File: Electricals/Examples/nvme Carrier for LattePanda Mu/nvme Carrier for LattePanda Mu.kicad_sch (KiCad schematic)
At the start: 8 parts

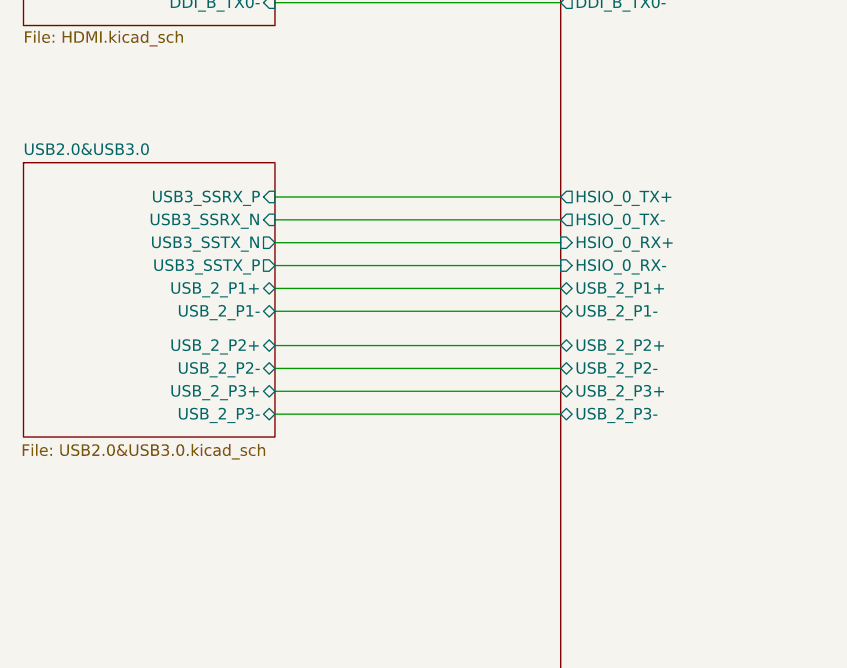
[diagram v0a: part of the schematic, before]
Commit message: Layout optimization + internal USB
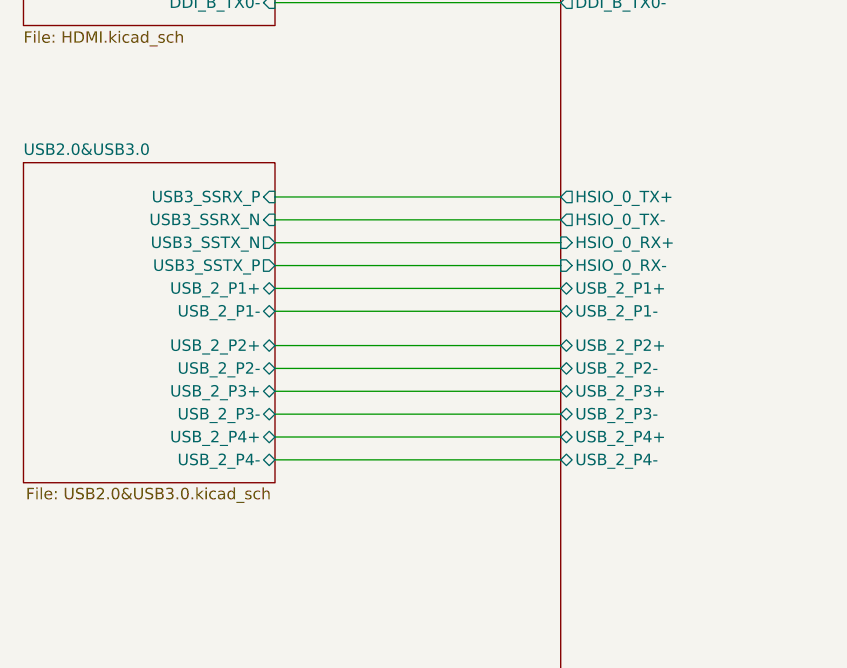
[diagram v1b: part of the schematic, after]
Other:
- sheet LattePanda Module ports: added USB_2_P4+, USB_2_P4-; removed none
- sheet USB2.0&USB3.0 ports: added USB_2_P4+, USB_2_P4-; removed none
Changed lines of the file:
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@@
 	(wire
 		(pts
+			(xy 195.58 242.57) (xy 227.33 242.57)
+		)
+		(stroke
+			(width 0)
+			(type default)
+		)
+	)
+	(wire
+		(pts
 			(xy 227.33 186.69) (xy 195.58 186.69)
 		)
@@
 	(wire
 		(pts
+			(xy 195.58 240.03) (xy 227.33 240.03)
+		)
+		(stroke
+			(width 0)
+			(type default)
+		)
+	)
+	(wire
+		(pts
 			(xy 227.33 184.15) (xy 195.58 184.15)
 		)
@@
 			)
 		)
+		(pin "USB_2_P4+" bidirectional
+			(at 227.33 240.03 180)
+			(effects
+				(font
+					(size 1.27 1.27)
+				)
+				(justify left)
+			)
+		)
+		(pin "USB_2_P4-" bidirectional
+			(at 227.33 242.57 180)
+			(effects
+				(font
+					(size 1.27 1.27)
+				)
+				(justify left)
+			)
+		)
 		(instances
 			(project "nvme Carrier for LattePanda Mu"
@@
 	(sheet
 		(at 167.64 209.55)
-		(size 27.94 30.48)
+		(size 27.94 35.56)
 		(stroke
 			(width 0.1524)
@@
 		)
 		(property "Sheetfile" "USB2.0&USB3.0.kicad_sch"
-			(at 167.386 240.792 0)
+			(at 167.894 245.618 0)
 			(effects
 				(font
@@
 			(effects
 				(font
+					(size 1.27 1.27)
+				)
+				(justify right)
+			)
+		)
+		(pin "USB_2_P4-" bidirectional
+			(at 195.58 242.57 0)
+			(effects
+				(font
+					(size 1.27 1.27)
+				)
+				(justify right)
+			)
+		)
+		(pin "USB_2_P4+" bidirectional
+			(at 195.58 240.03 0)
+			(effects
+				(font
